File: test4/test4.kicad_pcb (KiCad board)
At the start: 4 copper layers, 26.7 x 16.3 mm, 2 parts, among them U1 74LS245, U2 74LS245

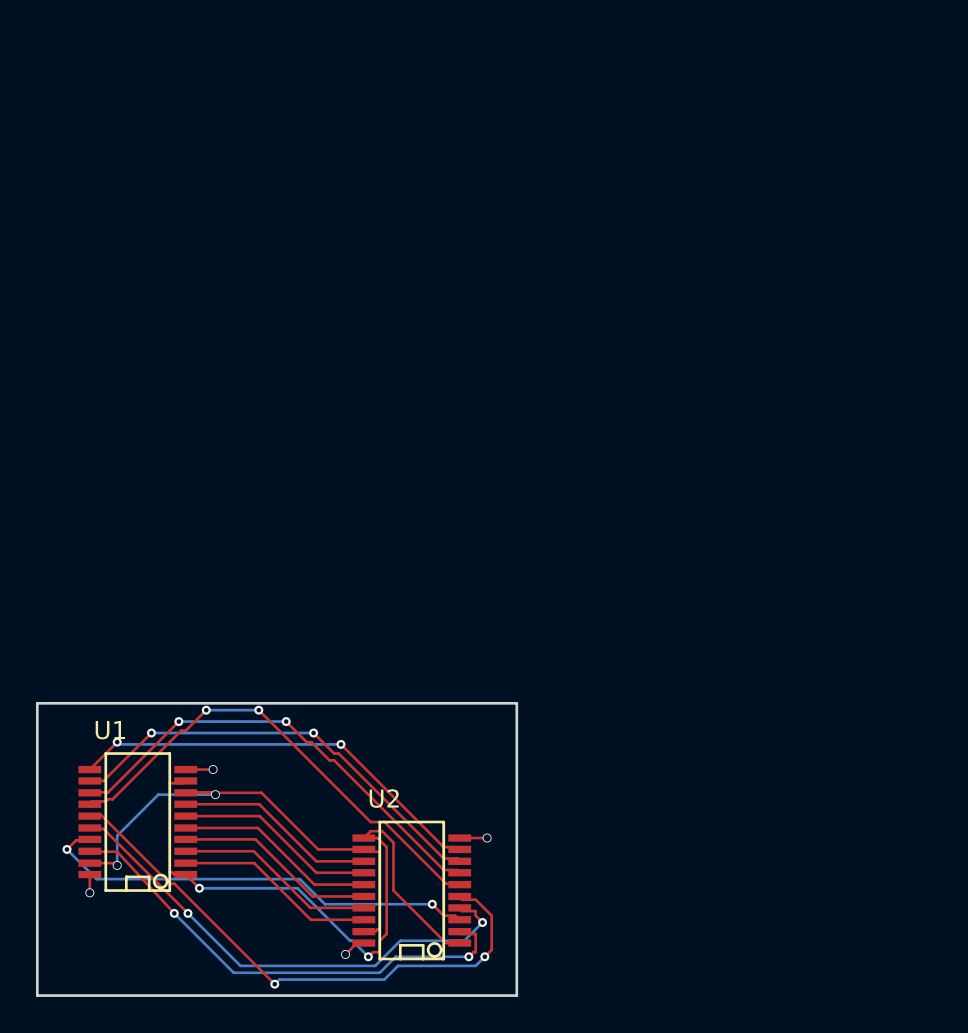
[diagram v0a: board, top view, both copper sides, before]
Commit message: adding schematic pseudo-symbol for AD9361
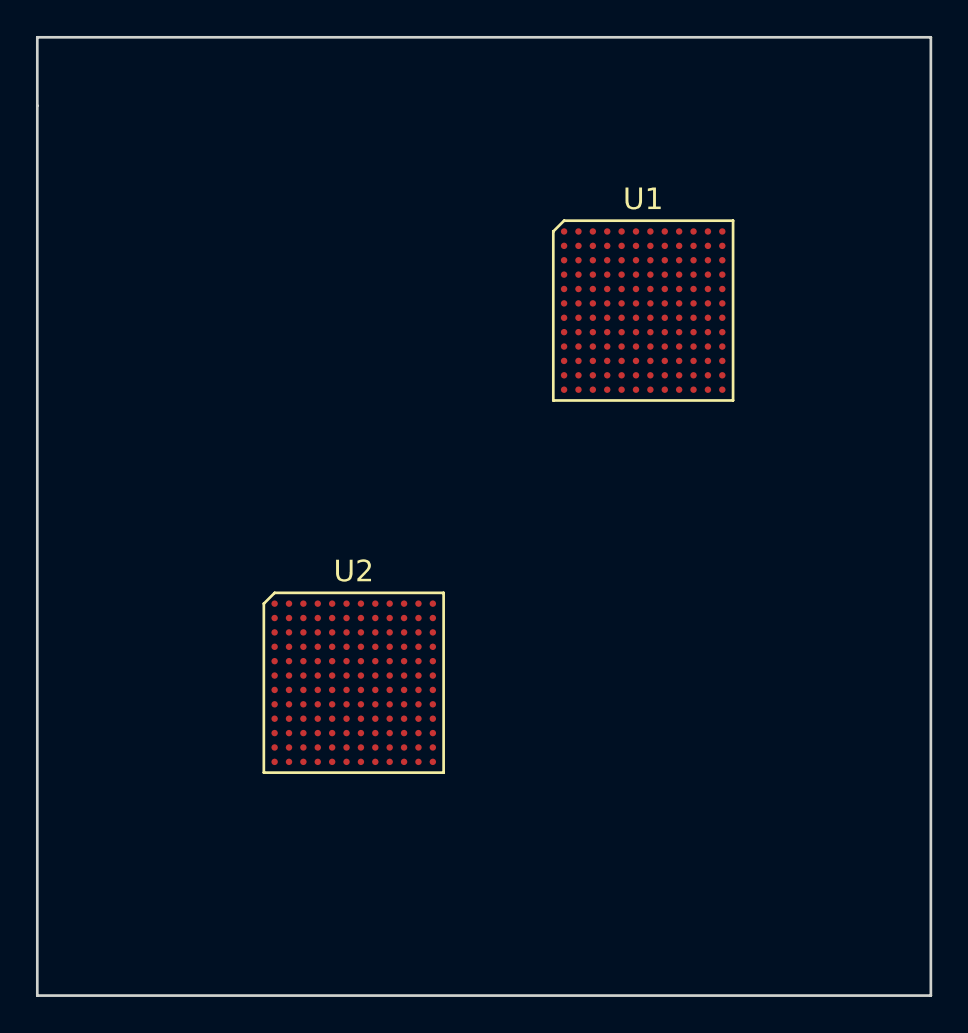
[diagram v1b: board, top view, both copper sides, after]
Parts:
- U1, U2: value 74LS245 -> AD9361; footprint SMD_Packages:SSOP-20 -> footprintlib:AD9361
- moved U1 40.0 mm to (162.7, 69.1), turned to 0 degrees
- moved U2 12.0 mm to (146.6, 89.8), turned to 0 degrees
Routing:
- net Net-(U1-Pad1): track 36.7 -> 0.00 mm, vias 2 -> 0
- net Net-(U1-Pad15): track 31.2 -> 0.00 mm, vias 2 -> 0
- net Net-(U1-Pad19): track 28.7 -> 0.00 mm, vias 2 -> 0
- net Net-(U1-Pad16): track 27.8 -> 0.00 mm, vias 2 -> 0
- net Net-(U1-Pad14): track 26.8 -> 0.00 mm, vias 2 -> 0
- net Net-(U1-Pad18): track 26.8 -> 0.00 mm, vias 2 -> 0
- net Net-(U1-Pad13): track 25.7 -> 0.00 mm, vias 2 -> 0
- net Net-(U1-Pad17): track 25.0 -> 0.00 mm, vias 2 -> 0
- net Net-(U1-Pad12): track 24.6 -> 0.00 mm, vias 2 -> 0
- net Net-(U1-Pad11): track 23.7 -> 0.00 mm, vias 2 -> 0
- net Net-(U1-Pad4): track 11.2 -> 0.00 mm
- net Net-(U1-Pad7): track 11.2 -> 0.00 mm
- net Net-(U1-Pad6): track 11.2 -> 0.00 mm
- net Net-(U1-Pad2): track 11.2 -> 0.00 mm
- net Net-(U1-Pad5): track 11.2 -> 0.00 mm
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- added copper zone on In5.Cu, net +3V3
- added copper zone on In6.Cu, net GND
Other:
- board size 26.7 x 16.3 mm -> 49.7 x 53.3 mm
- copper layers 4 -> 8
- net class Default: clearance 0.15 -> 0.127; trace_width 0.15 -> 0.127; via_dia 0.5 -> 0.3048; via_drill 0.4 -> 0.2032
- rule trace_clearance: 0.15 -> 0.127
- rule trace_min: 0.15 -> 0.127
- rule via_min_drill: 0.3 -> 0.1524
- rule via_min_size: 0.4 -> 0.254

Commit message: working with the AD9361 BGA fanout
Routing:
- net Net-(U1-PadM11): track 0.00 -> 30.8 mm, vias 0 -> 2
- net Net-(U1-PadM12): track 0.00 -> 30.8 mm, vias 0 -> 2
- net Net-(U1-PadL7): track 0.00 -> 17.0 mm, vias 0 -> 1
- net Net-(U1-PadL12): track 0.00 -> 11.4 mm
- net Net-(U1-PadL11): track 0.00 -> 10.5 mm
- net Net-(U1-PadK12): track 0.00 -> 8.78 mm
- net Net-(U1-PadJ11): track 0.00 -> 8.67 mm
- net Net-(U1-PadM2): track 0.00 -> 8.39 mm
- net Net-(U1-PadL2): track 0.00 -> 8.25 mm
- net Net-(U1-PadM6): track 0.00 -> 8.21 mm, vias 0 -> 1
- net Net-(U2-PadG6): track 0.00 -> 8.19 mm, vias 0 -> 1
- net Net-(U2-PadG7): track 0.00 -> 8.18 mm, vias 0 -> 1
- net Net-(U1-PadM7): track 0.00 -> 8.11 mm, vias 0 -> 1
- net Net-(U1-PadJ12): track 0.00 -> 8.07 mm
- net Net-(U2-PadG9): track 0.00 -> 8.03 mm, vias 0 -> 1
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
